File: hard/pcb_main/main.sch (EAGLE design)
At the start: 817 parts

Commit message: eskd fixes
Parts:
- removed S1: RESET, switch:4-1437565-2
- added SB1: RESET, switch:4-1437565-2
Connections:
- net GND: now also SB1.P, SB1.P1; no longer S1.P, S1.P1
- net RST: now also SB1.S, SB1.S1; no longer S1.S, S1.S1
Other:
- moved on the sheet: C1, C10, C11, C142, C143, C144, C145, C146, C147, C2, C3, C34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

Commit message: fixed busses for ESKD
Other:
- note added: "A(1)"
- note added: "A(2)"
- note added: "B(1,5,6,7,8)"
- note added: "B(1,5,6,7,9)"
- note added: "B(1,5,6,8,9)"
- note added: "B(1,5,7,8,9)"
- note added: "B(1,6,7,8,9)"
- note added: "B(5,6,7,8,9)"
- note added: "C(1,10)"
- note added: "C(3,10)"
- moved on the sheet: C100, C101, C102, C103, C104, C105, C106, C107, C108, C109, C110, C111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

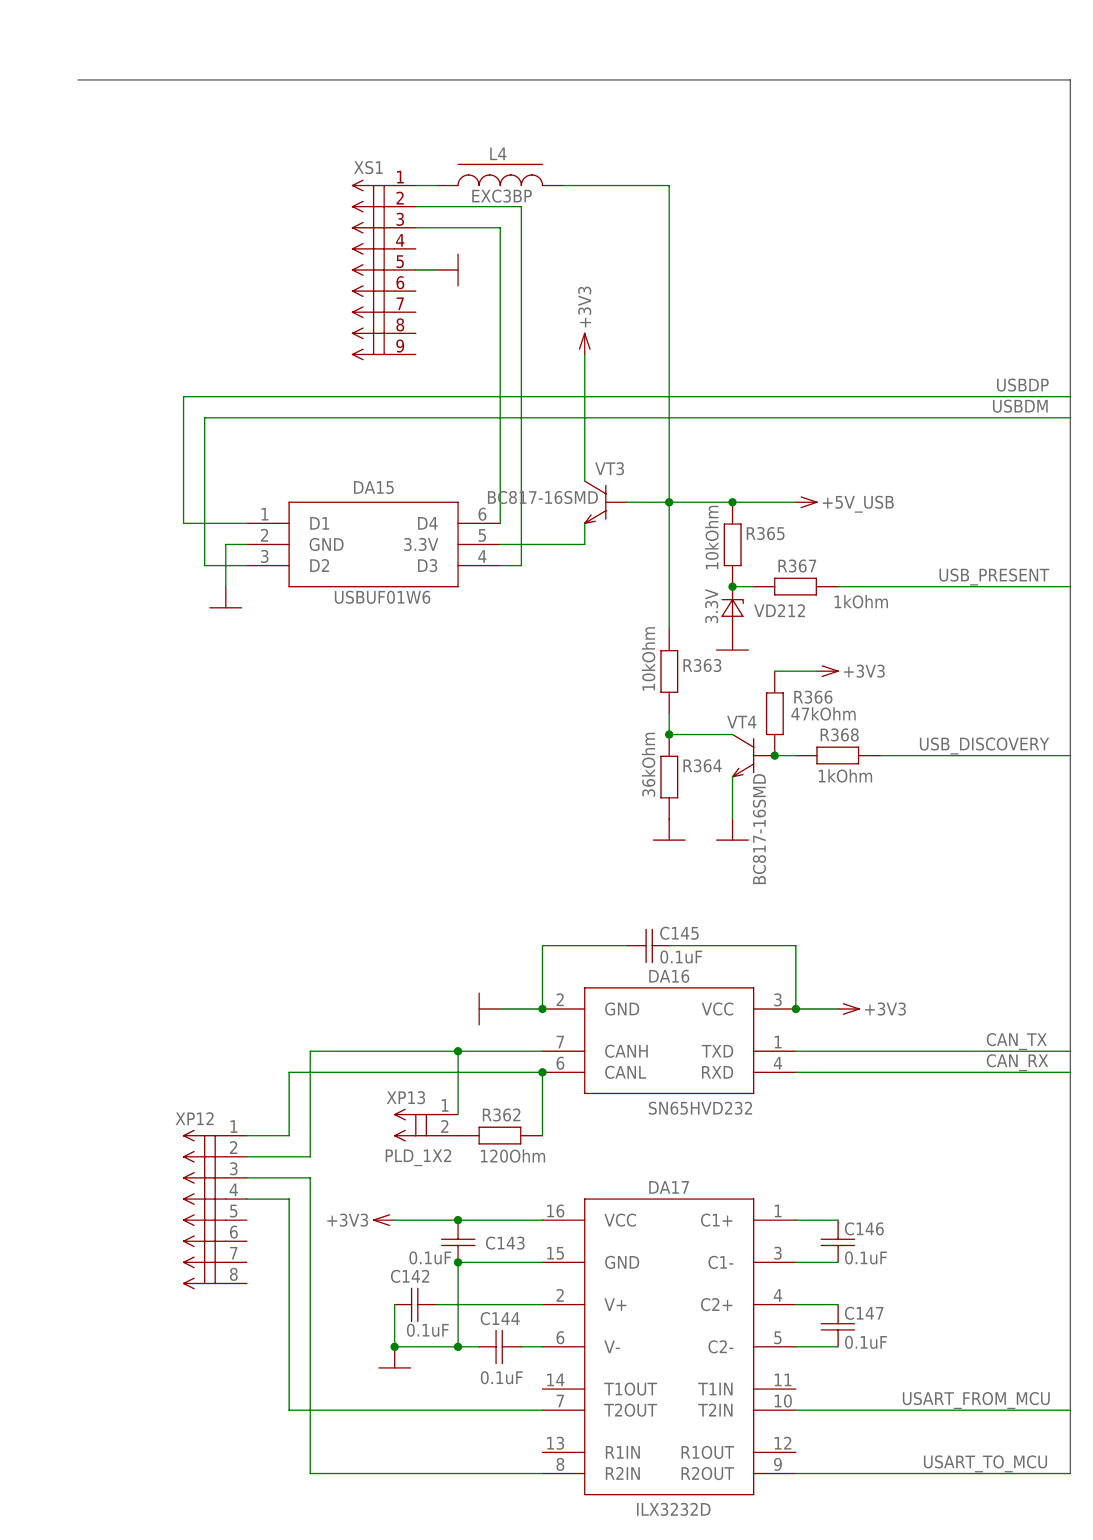
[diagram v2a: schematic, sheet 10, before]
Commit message: fixed busses for ESKD step 2
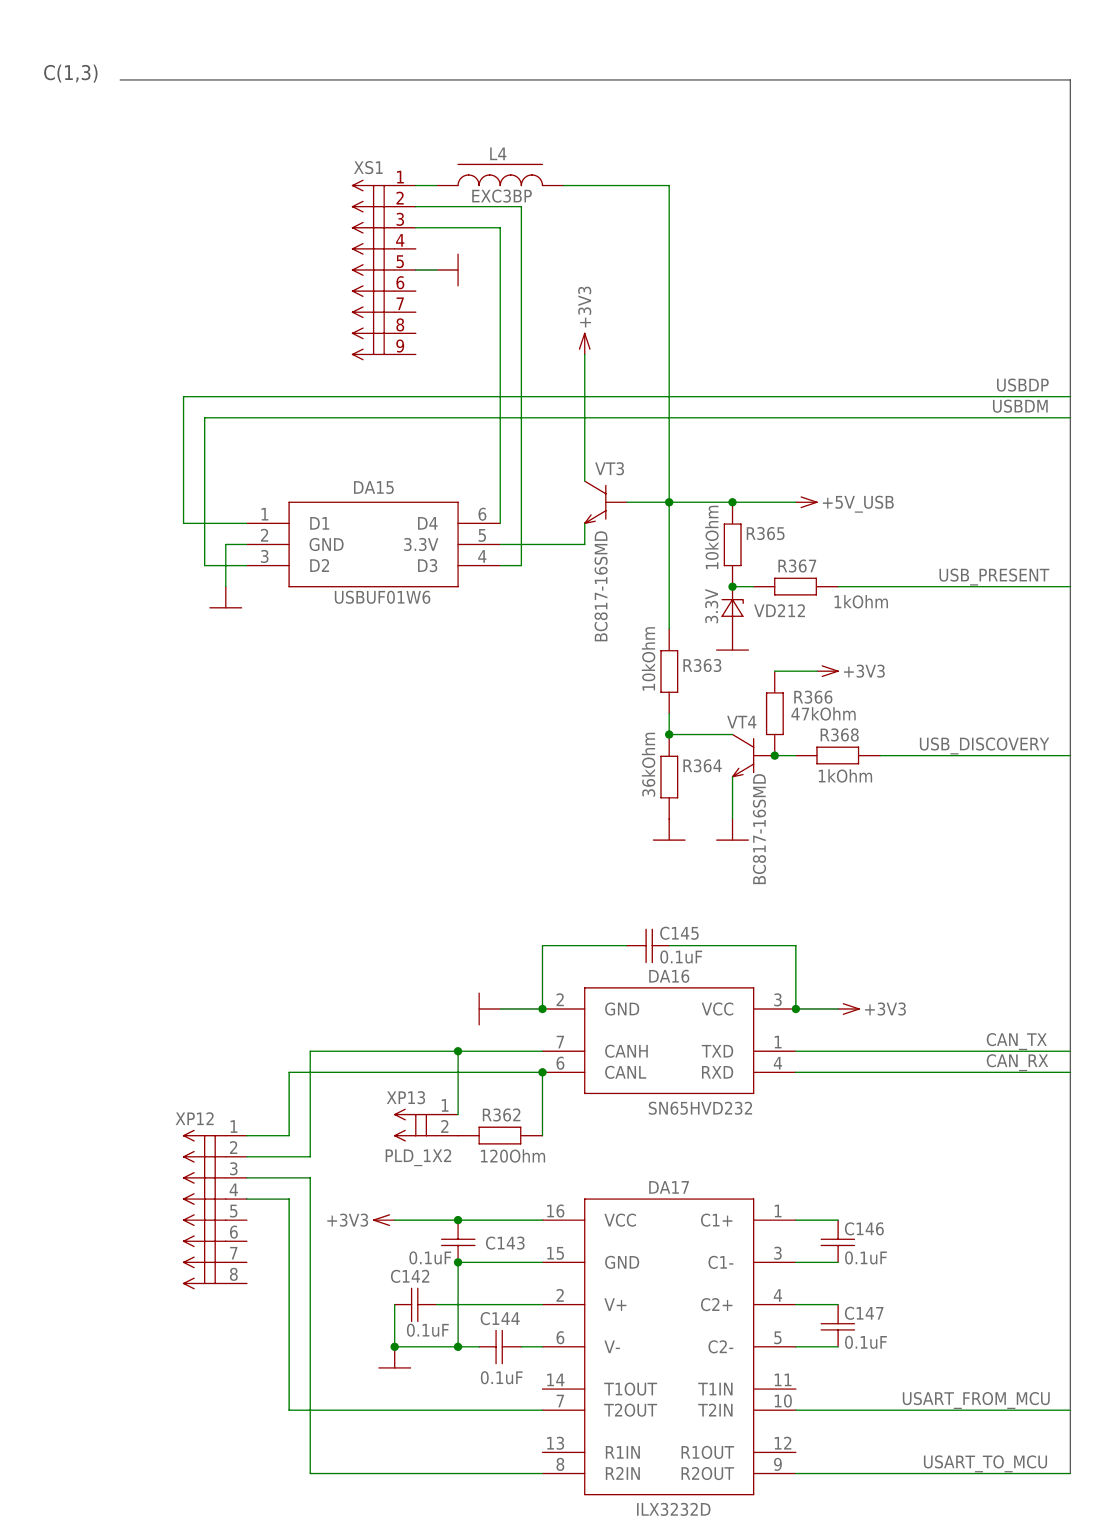
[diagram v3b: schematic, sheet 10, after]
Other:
- note added: "C(1,3)"
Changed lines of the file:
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@@
 <description>Interfaces</description>
 <plain>
+<text x="20.32" y="187.96" size="1.778" layer="92" rot="MR0">C(1,3)</text>
 </plain>
 <instances>
@@
 <attribute name="PARTNO" x="81.28" y="137.16" size="1.778" layer="96" rot="MR0" display="off"/>
 <attribute name="NAME" x="83.615" y="140.43" size="1.524" layer="95" rot="MR0"/>
-<attribute name="VALUE" x="80.44" y="136.97" size="1.524" layer="96" rot="MR0"/>
+<attribute name="VALUE" x="81.47" y="133.78" size="1.524" layer="96" rot="MR270"/>
 </instance>
 <instance part="R368" gate="G$1" x="109.22" y="106.68" smashed="yes">
@@
 <bus name="TACHOMETER,FREQMETER,SPEEDOMETER,USB_DISCOVERY,USB_PRESENT,USBDP,USBDM,USART_FROM_MCU,USART_TO_MCU,CAN_TX,CAN_RX">
 <segment>
-<wire x1="17.78" y1="187.96" x2="137.16" y2="187.96" width="0.762" layer="92"/>
+<wire x1="22.86" y1="187.96" x2="137.16" y2="187.96" width="0.762" layer="92"/>
 <wire x1="137.16" y1="187.96" x2="137.16" y2="20.32" width="0.762" layer="92"/>
 </segment>

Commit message: fixed frames for ESKD
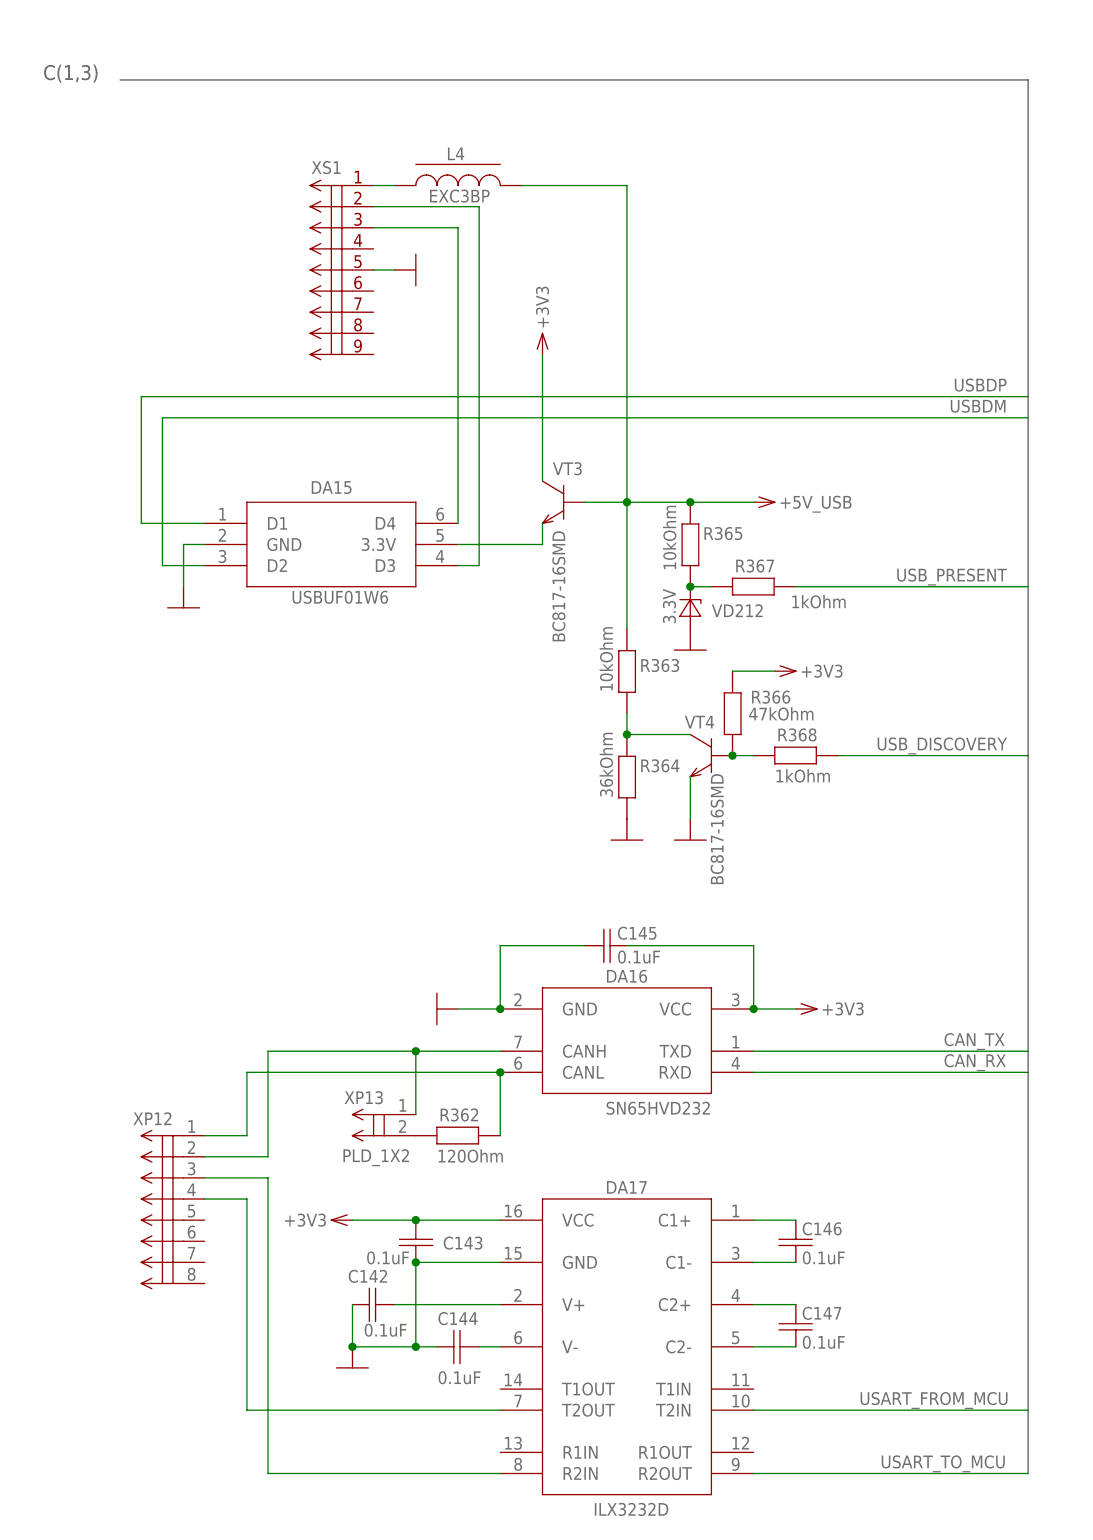
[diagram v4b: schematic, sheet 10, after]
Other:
- moved on the sheet: C142, C143, C144, C145, C146, C147, DA15, DA16, DA17, L4, R362, R363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

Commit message: nop
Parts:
- C3: value 0.1uF -> 10uF/10V; device rcl:C-EUC0603 -> rcl:CPOL-EUA/3216-18W; PARTNO C0603C104K5RACTU -> T491A106K010AT
- C4: value 10uF/10V -> 22pF; device rcl:CPOL-EUA/3216-18W -> rcl:C-EUC0603; PARTNO T491A106K010AT -> C0603C220J5GACTU
- C59: value 0.01uF -> 0.1uF; PARTNO C0603C103K5RACTU -> C0603C104K5RACTU
- C6: value 22pF -> 0.1uF; PARTNO C0603C220J5GACTU -> C0603C104K5RACTU
- C60: value 0.1uF -> 10uF/50V; device rcl:C-EUC0603 -> rcl:C-EUC2220K; PARTNO C0603C104K5RACTU -> 22205C106KAT2A
- C61: value 10uF/50V -> 0.1uF; device rcl:C-EUC2220K -> rcl:C-EUC0603; PARTNO 22205C106KAT2A -> C0603C104K5RACTU
- C62: value 0.1uF -> 0.01uF; PARTNO C0603C104K5RACTU -> C0603C103K5RACTU
- R10: value 0Ohm -> 10kOhm; device rcl:R-EU_R0805 -> rcl:R-EU_R0603; PARTNO ERJ6GEY0R00V -> RC0603FR-1010KL
- R8: value 10kOhm -> 0Ohm; device rcl:R-EU_R0603 -> rcl:R-EU_R0805; PARTNO RC0603FR-1010KL -> ERJ6GEY0R00V
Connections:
- net +24V_CLEAR: now also C59.1, C60.2, C61.1; no longer C60.1, C61.2, C62.1
- net +3V3: now also C2.1, C3.+, R10.2; no longer C3.1, C4.+, R8.2
- net AGND: now also R8.2; no longer R10.2
- net GND: now also C3.-, C4.2, C60.1, C62.2, R8.1; no longer C3.2, C4.-, C60.2, C61.1, R10.1
- net JTDO: now also R9.1; no longer R8.1
- net N$14: now also C5.1; no longer C6.1
- net N$15: now also C4.1; no longer C5.1
- net N$28: now also C62.1; no longer C59.1
- net N$86: now also C61.2; no longer C62.2
- net RST: now also C6.1, R10.1; no longer C2.1, R9.1
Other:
- moved on the sheet: C2, C5, C56, C57, C58, C59, C6, C60, C61, C62, C64, C65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

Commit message: before resizing board
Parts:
- added Z2: NFE31PT, emi-filter:NFE31PT
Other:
- moved on the sheet: C1, C10, C11, C2, C3, C4, C5, C6, C7, C8, C9, DD1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

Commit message: moved to different board
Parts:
- removed Z2: NFE31PT, emi-filter:NFE31PT
- added JP7, JP8: STAND-OFF-M4, mount:STAND-OFF-M4
- JP1, JP2, JP3, JP4, JP5, JP6: value STAND-OFFLONG -> STAND-OFF-M4; device mount:STAND-OFFLONG -> mount:STAND-OFF-M4; BOM EXCLUDE -> (none)
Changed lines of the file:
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@@
 <attribute name="PARTNO" value="TCMT4100"/>
 </part>
-<part name="JP1" library="mount" deviceset="STAND-OFF" device="LONG">
-<attribute name="BOM" value="EXCLUDE"/>
-</part>
-<part name="JP2" library="mount" deviceset="STAND-OFF" device="LONG">
-<attribute name="BOM" value="EXCLUDE"/>
-</part>
-<part name="JP3" library="mount" deviceset="STAND-OFF" device="LONG">
-<attribute name="BOM" value="EXCLUDE"/>
-</part>
-<part name="JP4" library="mount" deviceset="STAND-OFF" device="LONG">
-<attribute name="BOM" value="EXCLUDE"/>
-</part>
-<part name="JP5" library="mount" deviceset="STAND-OFF" device="LONG">
-<attribute name="BOM" value="EXCLUDE"/>
-</part>
-<part name="JP6" library="mount" deviceset="STAND-OFF" device="LONG">
-<attribute name="BOM" value="EXCLUDE"/>
-</part>
 <part name="XP8" library="connector" deviceset="MOLEX-90130-*16" device="">
 <attribute name="LABEL" value="DISCRETE(17..32)"/>
@@
 </part>
 <part name="U$1" library="frame-simplified" deviceset="A1_PORTRAIT_NEXT_SCALED" device=""/>
-<part name="Z2" library="emi-filter" deviceset="NFE31PT" device=""/>
+<part name="JP1" library="mount" deviceset="STAND-OFF-*" device="" technology="M4"/>
+<part name="JP2" library="mount" deviceset="STAND-OFF-*" device="" technology="M4"/>
+<part name="JP3" library="mount" deviceset="STAND-OFF-*" device="" technology="M4"/>
+<part name="JP4" library="mount" deviceset="STAND-OFF-*" device="" technology="M4"/>
+<part name="JP5" library="mount" deviceset="STAND-OFF-*" device="" technology="M4"/>
+<part name="JP6" library="mount" deviceset="STAND-OFF-*" device="" technology="M4"/>
+<part name="JP7" library="mount" deviceset="STAND-OFF-*" device="" technology="M4"/>
+<part name="JP8" library="mount" deviceset="STAND-OFF-*" device="" technology="M4"/>
 </parts>
 <sheets>
@@
 <attribute name="VALUE" x="316.23" y="86.948" size="1.524" layer="96" rot="MR0"/>
 </instance>
-<instance part="Z2" gate="G$1" x="401.32" y="175.26"/>
 </instances>
 <busses>
@@
 </plain>
 <instances>
-<instance part="JP1" gate="G$1" x="0" y="48.26" smashed="yes">
-<attribute name="BOM" value="EXCLUDE" x="0" y="48.26" size="1.524" layer="96" display="off"/>
-</instance>
-<instance part="JP2" gate="G$1" x="0" y="40.64" smashed="yes">
-<attribute name="BOM" value="EXCLUDE" x="0" y="40.64" size="1.524" layer="96" display="off"/>
-</instance>
-<instance part="JP3" gate="G$1" x="0" y="33.02" smashed="yes">
-<attribute name="BOM" value="EXCLUDE" x="0" y="33.02" size="1.524" layer="96" display="off"/>
-</instance>
-<instance part="JP4" gate="G$1" x="0" y="25.4" smashed="yes">
-<attribute name="BOM" value="EXCLUDE" x="0" y="25.4" size="1.524" layer="96" display="off"/>
-</instance>
-<instance part="JP5" gate="G$1" x="0" y="17.78" smashed="yes">
-<attribute name="BOM" value="EXCLUDE" x="0" y="17.78" size="1.524" layer="96" display="off"/>
-</instance>
-<instance part="JP6" gate="G$1" x="0" y="10.16" smashed="yes">
-<attribute name="BOM" value="EXCLUDE" x="0" y="10.16" size="1.524" layer="96" display="off"/>
-</instance>
+<instance part="JP1" gate="G$1" x="0" y="2.54"/>
+<instance part="JP2" gate="G$1" x="0" y="7.62"/>
+<instance part="JP3" gate="G$1" x="0" y="12.7"/>
+<instance part="JP4" gate="G$1" x="0" y="17.78"/>
+<instance part="JP5" gate="G$1" x="0" y="22.86"/>
+<instance part="JP6" gate="G$1" x="0" y="27.94"/>
+<instance part="JP7" gate="G$1" x="0" y="33.02"/>
+<instance part="JP8" gate="G$1" x="0" y="38.1"/>
 </instances>
 <busses>
